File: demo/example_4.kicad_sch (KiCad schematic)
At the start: 10 parts, among them U3 ISL91127IR

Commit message: Update demo project for upcoming changes
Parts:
- C5, C6, R17: KiVar.Rule ISL91127 IRNZ(-!) -> (none); Var (none) -> ISL91127 IRNZ(-!)
- R16: KiVar.Rule ISL91127 IRNZ(0Ω) IRAZ(1MΩ) -> (none); Var (none) -> ISL91127 IRNZ(0Ω) IRAZ(1MΩ)
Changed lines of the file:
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@@
 	(title_block
 		(title "KiVar Demo")
-		(date "2024-03-18")
+		(date "2024-03-19")
 		(company "Author: Mark Hämmerling <dev@markh.de>")
 		(comment 1 "https://github.com/markh-de/KiVar")
@@
 			)
 		)
-		(property "KiVar.Rule" "ISL91127 IRNZ(0Ω) IRAZ(1MΩ)"
+		(property "Var" "ISL91127 IRNZ(0Ω) IRAZ(1MΩ)"
 			(at 186.69 90.1699 0)
 			(effects
@@
 		(fields_autoplaced yes)
 		(property "Reference" "U3"
-			(at 104.8894 76.2 0)
+			(at 105.0641 76.2 0)
 			(effects
 				(font
@@
 		)
 		(property "Value" "ISL91127IR"
-			(at 104.8894 78.74 0)
+			(at 105.0641 78.74 0)
 			(effects
 				(font
@@
 				)
 				(hide yes)
-			)
-		)
-		(property "KiVar.Rule" ""
-			(at 99.06 90.17 0)
-			(effects
-				(font
-					(size 1.27 1.27)
-				)
 			)
 		)
@@
 		(on_board yes)
 		(dnp no)
+		(fields_autoplaced yes)
 		(property "Reference" "C6"
 			(at 158.75 85.0899 0)
@@
 			)
 		)
-		(property "KiVar.Rule" "ISL91127 IRNZ(-!)"
+		(property "Var" "ISL91127 IRNZ(-!)"
 			(at 158.75 90.1699 0)
 			(effects
@@
 			)
 		)
-		(property "KiVar.Rule" "ISL91127 IRNZ(-!)"
+		(property "Var" "ISL91127 IRNZ(-!)"
 			(at 186.69 97.7899 0)
 			(effects
@@
 			)
 		)
-		(property "KiVar.Rule" "ISL91127 IRNZ(-!)"
+		(property "Var" "ISL91127 IRNZ(-!)"
 			(at 128.27 90.1699 0)
 			(effects
@@
 		)
 		(property "Value" "GND"
-			(at 184.15 104.14 0)
-			(effects
-				(font
-					(size 1.27 1.27)
-				)
+			(at 186.69 100.3299 0)
+			(effects
+				(font
+					(size 1.27 1.27)
+				)
+				(justify left)
 			)
 		)
@@
 			)
 		)
-		(property "KiVar.Rule" ""
-			(at 99.06 73.66 0)
-			(effects
-				(font
-					(size 1.27 1.27)
-				)
-			)
-		)

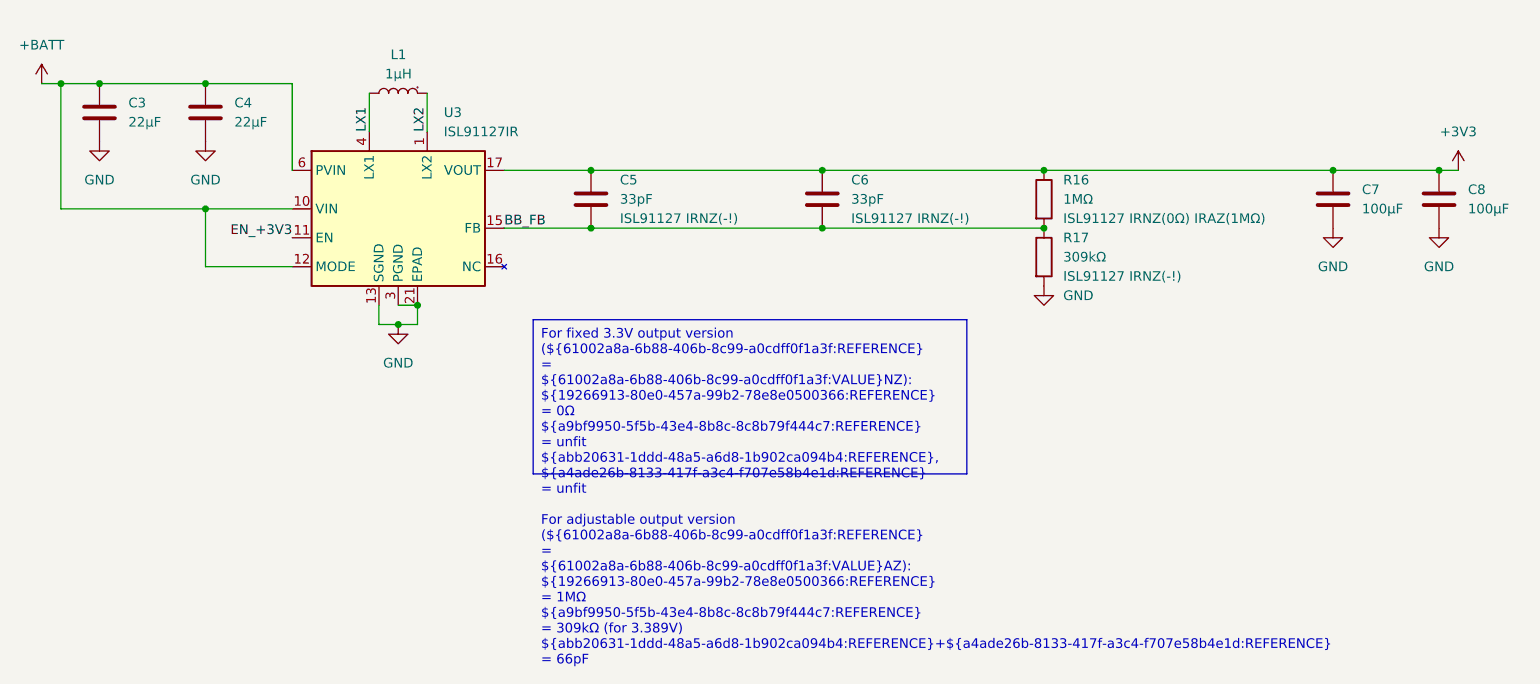
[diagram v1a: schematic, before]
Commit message: Make use of new 0.2.0 features in demo project, use different expression types
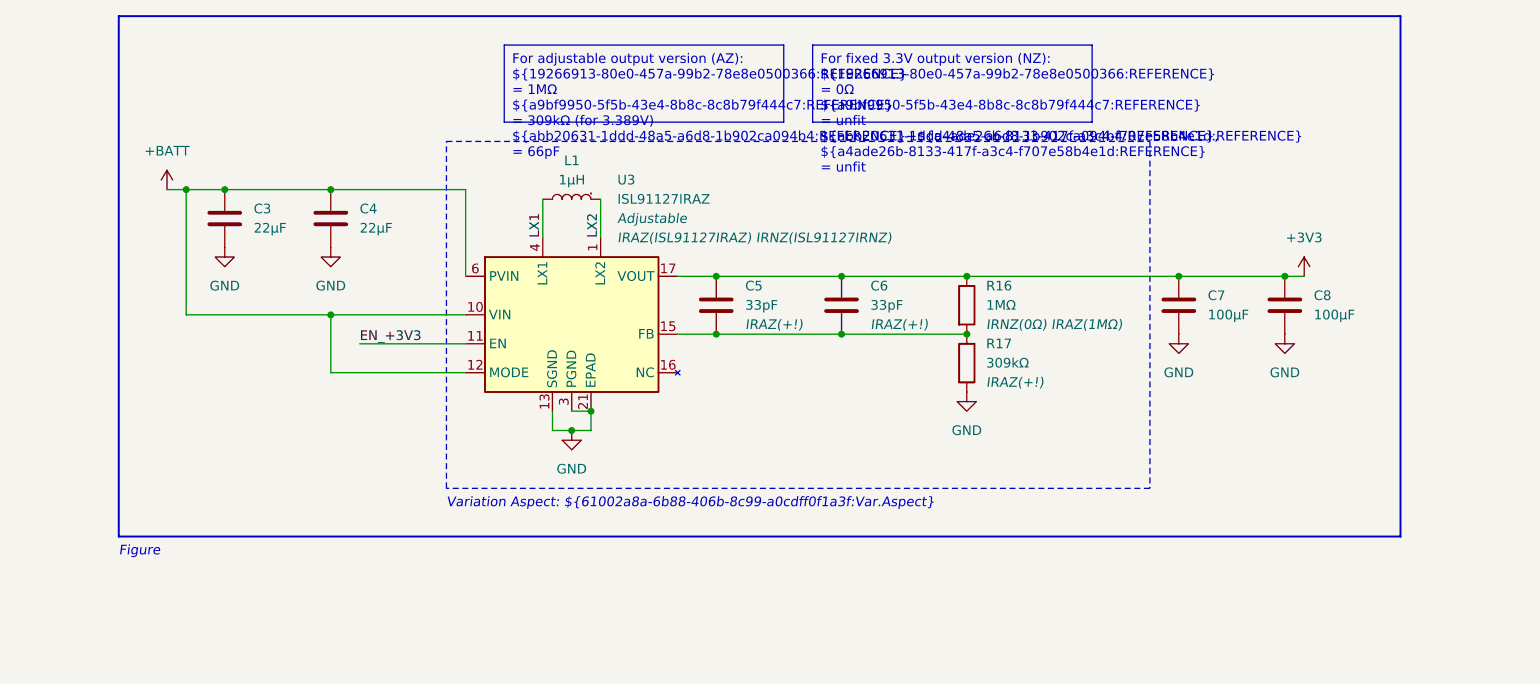
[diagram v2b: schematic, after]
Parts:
- C5, C6, R17: Var ISL91127 IRNZ(-!) -> IRAZ(+!); Var.Aspect (none) -> ISL91127
- R16: Var ISL91127 IRNZ(0Ω) IRAZ(1MΩ) -> IRNZ(0Ω) IRAZ(1MΩ); Var.Aspect (none) -> ISL91127
- U3: value ISL91127IR -> ISL91127IRAZ; Info (none) -> Adjustable; Info.Var (none) -> IRAZ(Adjustable) IRNZ(Fixed); MPN (none) -> ISL91127IRAZ-T7A; MPN.Var (none) -> IRAZ(ISL91127IRAZ-T7A) IRNZ(ISL91127IRNZ-T7A); Manufacturer (none) -> Renesas Electronics Corporation; Var (none) -> IRAZ(ISL91127IRAZ) IRNZ(ISL91127IRNZ); Var.Aspect (none) -> ISL91127
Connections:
- net BB_FB: no longer names the net of C5.2, C6.2, R16.2, R17.1, U3.15 (FB)
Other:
- note added: "Figure"
- note added: "Variation Aspect: ${61002a8a-6b88-406b-8c99-a0cdff0f1a3f:Var.Aspect}"
- moved on the sheet: C3, C4, C5, C6, C7, C8, L1, R16, R17, U3
